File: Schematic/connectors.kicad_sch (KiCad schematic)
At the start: 36 parts, among them J10 PIN2216, J11 PIN2216, J12 PIN2216, J2 PIN2216, J3 PIN2216, J4 PIN2216, J5 PIN2216, J6 PIN2216, J7 PIN2216, J8 PIN2216, J9 PIN2216, U14 HDGC1002WR-S-4P, U15 HDGC1002WR-S-4P, U16 HDGC1002WR-S-4P, U17 HDGC1002WR-S-4P, U18 HDGC1002WR-S-4P, U19 HDGC1002WR-S-4P, U20 HDGC1002WR-S-4P, U21 HDGC1002WR-S-8P, U22 HDGC1002WR-S-8P, U23 HDGC1002WR-S-6P, U24 HDGC1002WR-S-6P

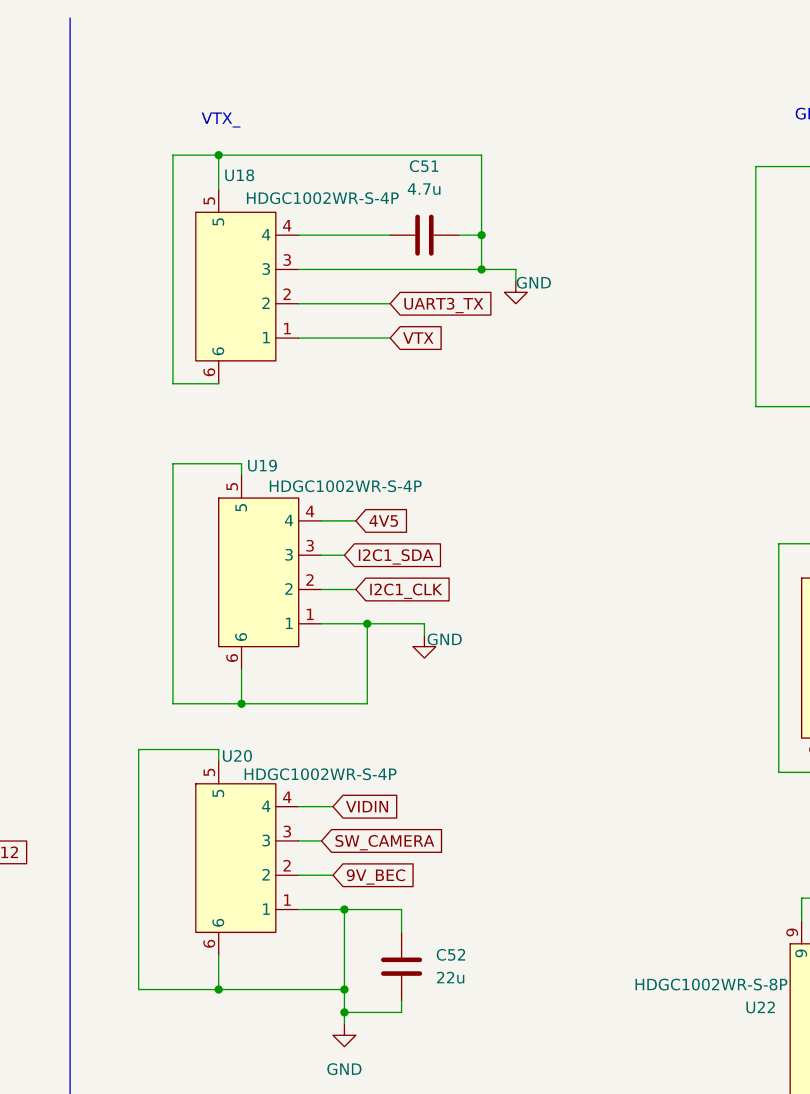
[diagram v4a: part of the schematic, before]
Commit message: Refactor schematic files and update component placements
- Adjusted component positions in osd.kicad_sch for better layout.
- Added new junctions and wires in rf_rx.kicad_sch to improve connectivity.
- Introduced additional junctions and wires in sensors.kicad_sch for enhanced signal routing.
- Removed outdated backup file fch7-2025-11-18_191836.zip and added new backup fch7-2025-11-27_202230.zip.
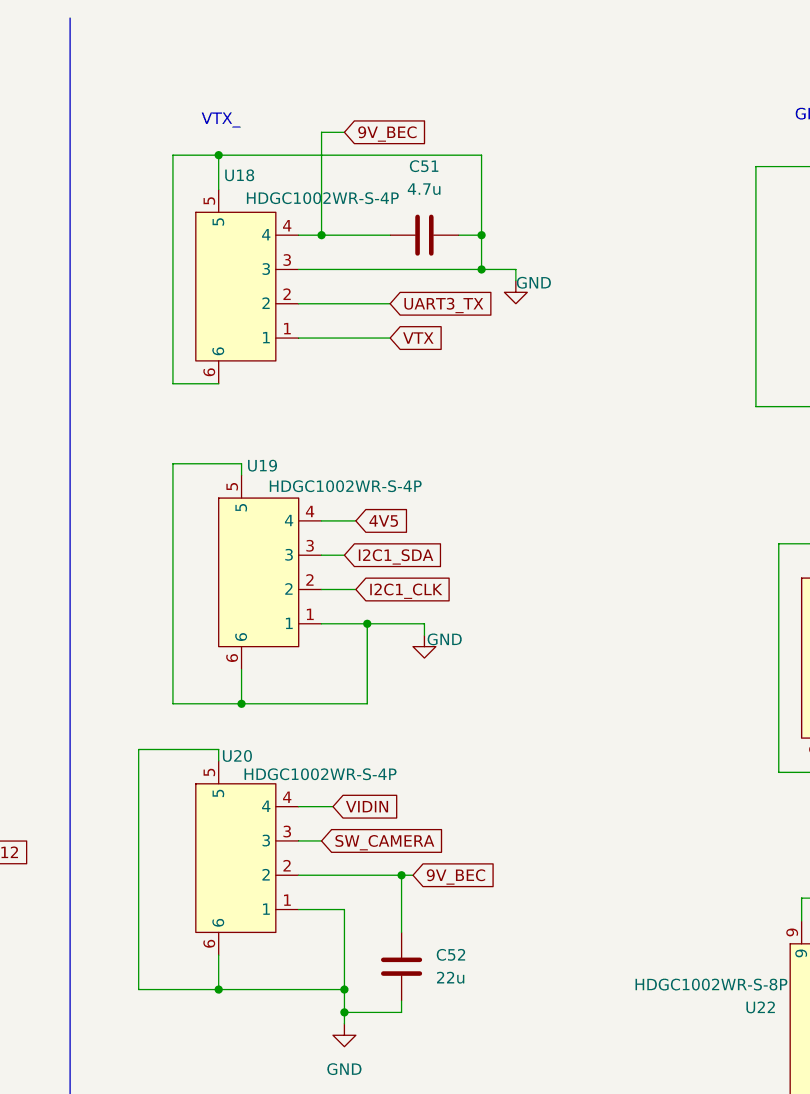
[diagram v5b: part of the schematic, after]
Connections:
- net 9V_BEC: now also C51.1, C52.2, U18.4
- net GND: no longer C52.2
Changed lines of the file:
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@@
-	)
-	(junction
-		(at 147.32 111.76)
-		(diameter 0)
-		(color 0 0 0 0)
 	)
 	(junction
@@
 	)
 	(junction
+		(at 144.78 36.83)
+		(diameter 0)
+		(color 0 0 0 0)
+	)
+	(junction
+		(at 153.67 107.95)
+		(diameter 0)
+		(color 0 0 0 0)
+	)
+	(junction
 		(at 31.75 87.63)
 		(diameter 0)
@@
 	(wire
 		(pts
-			(xy 153.67 111.76) (xy 153.67 114.3)
+			(xy 153.67 107.95) (xy 153.67 114.3)
 		)
 		(stroke
@@
 	(wire
 		(pts
+			(xy 144.78 36.83) (xy 152.4 36.83)
+		)
+		(stroke
+			(width 0)
+			(type default)
+		)
+	)
+	(wire
+		(pts
 			(xy 207.01 121.92) (xy 208.28 121.92)
 		)
@@
 	(wire
 		(pts
+			(xy 147.32 25.4) (xy 144.78 25.4)
+		)
+		(stroke
+			(width 0)
+			(type default)
+		)
+	)
+	(wire
+		(pts
 			(xy 210.82 90.17) (xy 212.09 90.17)
 		)
@@
 	(wire
 		(pts
-			(xy 142.24 107.95) (xy 146.05 107.95)
+			(xy 142.24 107.95) (xy 153.67 107.95)
 		)
 		(stroke
@@
 	(wire
 		(pts
+			(xy 144.78 25.4) (xy 144.78 36.83)
+		)
+		(stroke
+			(width 0)
+			(type default)
+		)
+	)
+	(wire
+		(pts
 			(xy 31.75 119.38) (xy 44.45 119.38)
 		)
@@
 	(wire
 		(pts
+			(xy 153.67 107.95) (xy 154.94 107.95)
+		)
+		(stroke
+			(width 0)
+			(type default)
+		)
+	)
+	(wire
+		(pts
 			(xy 153.67 143.51) (xy 153.67 146.05)
 		)
@@
 	(wire
 		(pts
-			(xy 142.24 36.83) (xy 152.4 36.83)
+			(xy 142.24 36.83) (xy 144.78 36.83)
 		)
 		(stroke
@@
 	(wire
 		(pts
-			(xy 147.32 111.76) (xy 153.67 111.76)
-		)
-		(stroke
-			(width 0)
-			(type default)
-		)
-	)
-	(wire
-		(pts
 			(xy 222.25 87.63) (xy 222.25 96.52)
 		)
@@
 		)
 	)
+	(global_label "9V_BEC"
+		(shape input)
+		(at 147.32 25.4 0)
+		(fields_autoplaced yes)
+		(effects
+			(font
+				(size 1.27 1.27)
+			)
+			(justify left)
+		)
+		(property "Intersheetrefs" "${INTERSHEET_REFS}"
+			(at 157.2599 25.4 0)
+			(effects
+				(font
+					(size 1.27 1.27)
+				)
+				(justify left)
+				(hide yes)
+			)
+		)
+	)
 	(global_label "SWD_SWCLK"
 		(shape input)
@@
 	(global_label "9V_BEC"
 		(shape input)
-		(at 146.05 107.95 0)
-		(fields_autoplaced yes)
-		(effects
-			(font
-				(size 1.27 1.27)
-			)
-			(justify left)
-		)
-		(property "Intersheetrefs" "${INTERSHEET_REFS}"
-			(at 155.9899 107.95 0)
-			(effects
-				(font
+		(at 154.94 107.95 0)
+		(fields_autoplaced yes)
+		(effects
+			(font
+				(size 1.27 1.27)
+			)
+			(justify left)
+		)
+		(property "Intersheetrefs" "${INTERSHEET_REFS}"
+			(at 164.8799 107.95 0)
+			(effects
+				(font

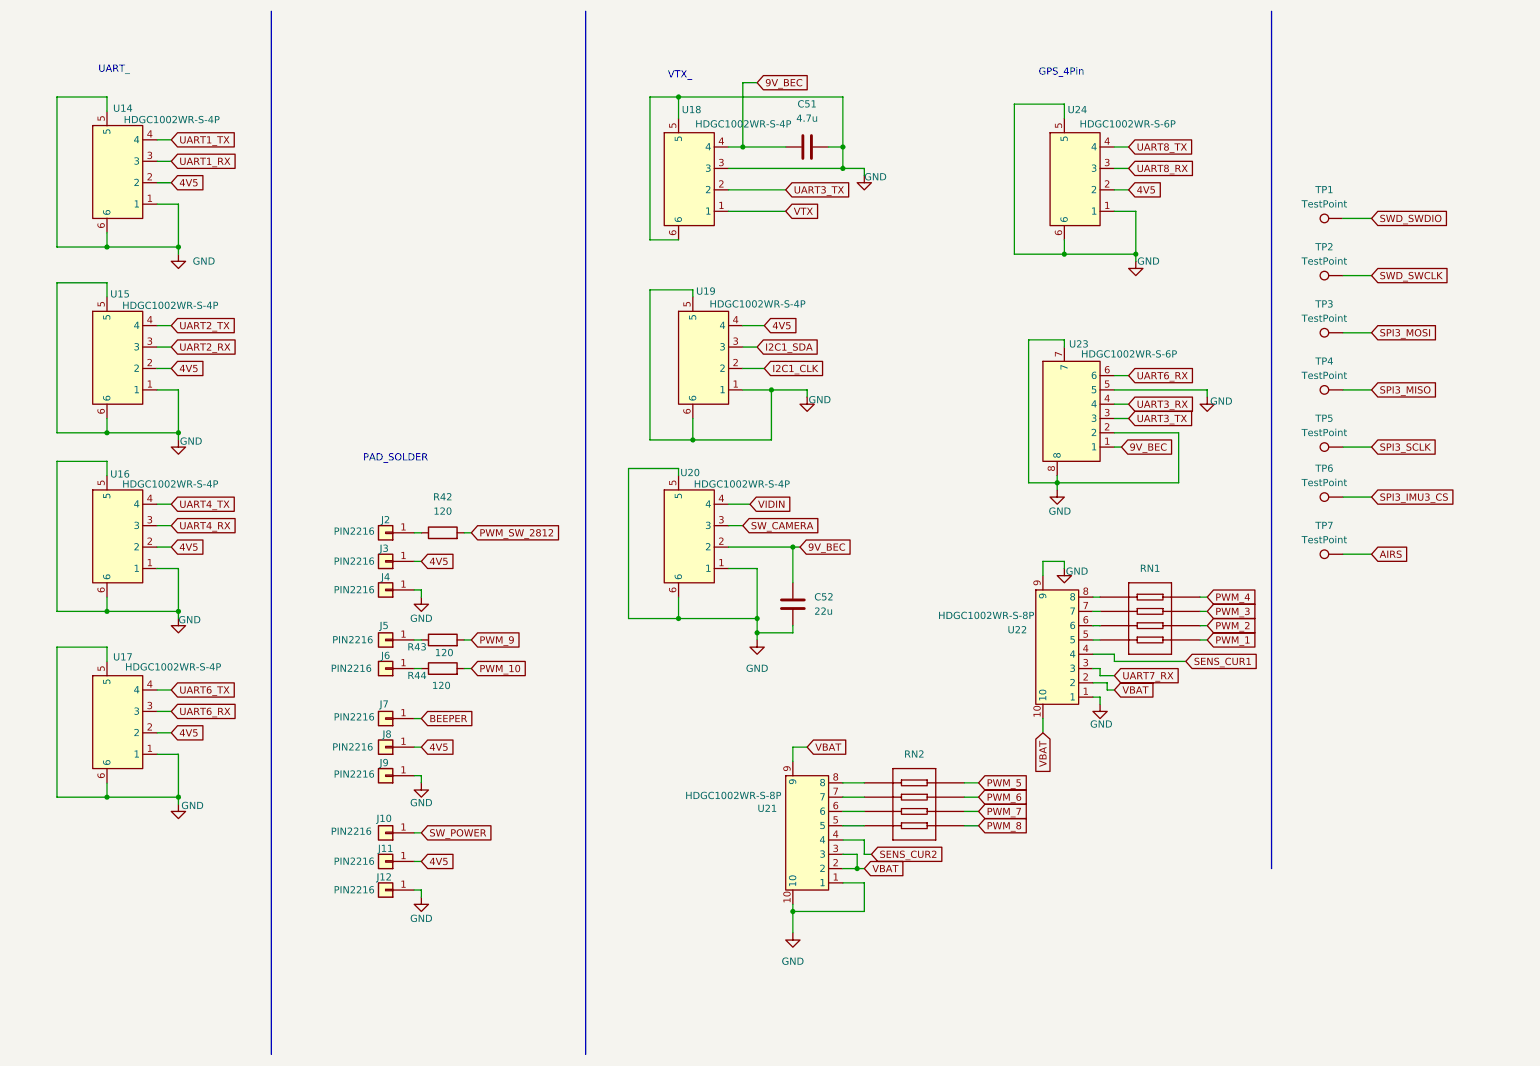
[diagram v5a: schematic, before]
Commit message: Removed useless analog OSD and VTX conneections to support only digital DJI
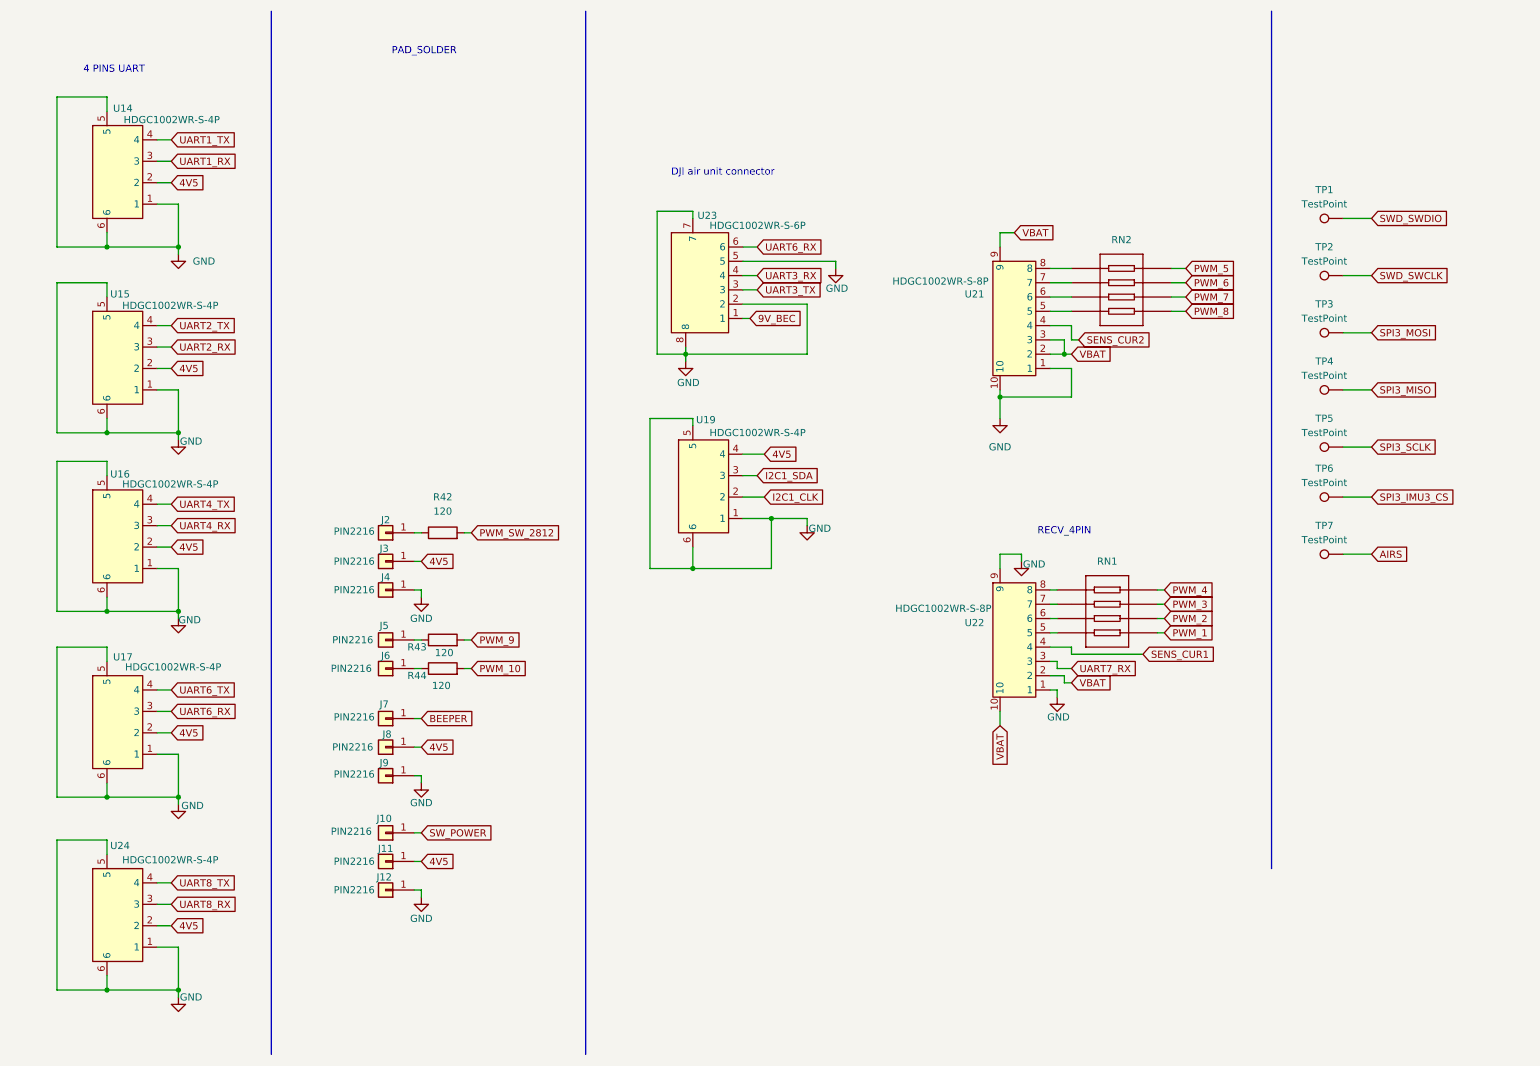
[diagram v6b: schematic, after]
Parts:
- removed C51: 4.7u, Capacitor_SMD:C_0603_1608Metric, symbol Device:C
- removed C52: 22u, Capacitor_SMD:C_0805_2012Metric, symbol Device:C
- removed U18, U20: HDGC1002WR-S-4P, fch7_fp:SM03B-SRSS-TB(LF)(SN), symbol fclib:HDGC1002WR-S-4P
- U24: value HDGC1002WR-S-6P -> HDGC1002WR-S-4P; footprint fch7_fp:CONN-SMD_HDGC1002WR-S-6P -> fch7_fp:SM03B-SRSS-TB(LF)(SN)
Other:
- note added: "4 PINS UART"
- note added: "DJI air unit connector"
- note added: "RECV_4PIN"
- note removed: "GPS_4Pin"
- note removed: "UART_"
- note removed: "VTX_"
- moved on the sheet: RN1, RN2, U19, U21, U22, U23, U24

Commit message: refactor : improve readability and portability of the project
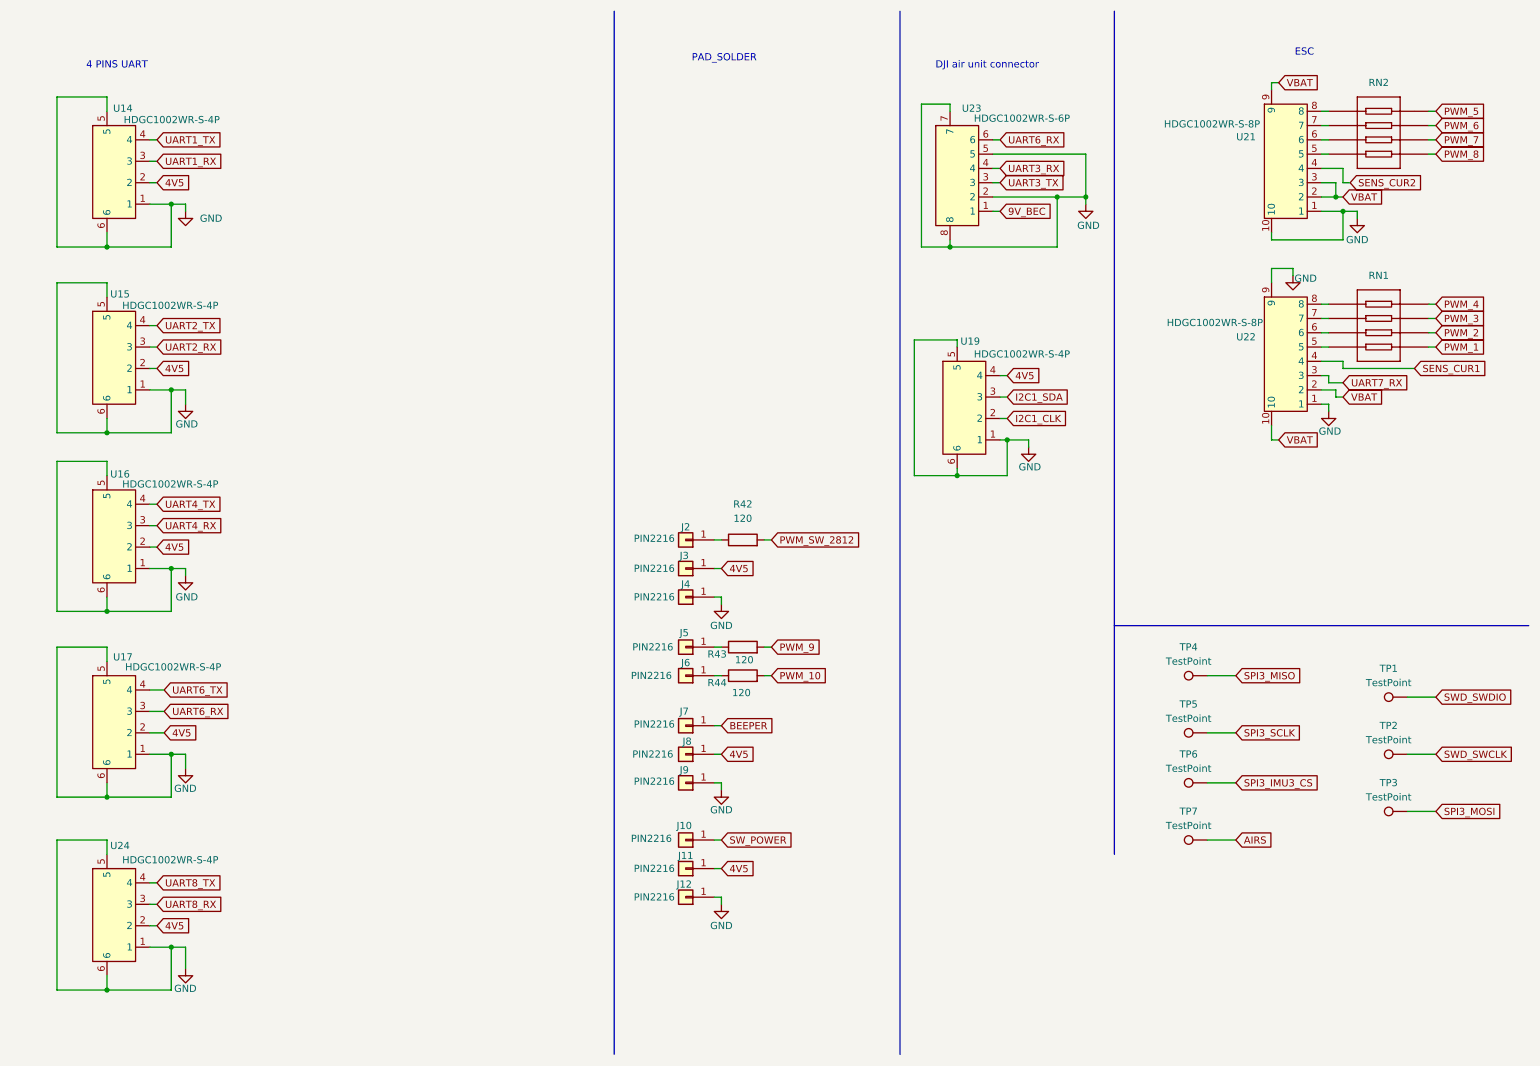
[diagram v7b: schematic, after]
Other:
- note added: "ESC"
- note removed: "RECV_4PIN"
- moved on the sheet: J10, J11, J12, J2, J3, J4, J5, J6, J7, J8, J9, R42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

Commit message: zdd :minor improvements
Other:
- note added: "Debugging"
- note added: "Vérifier l'ordre des pins pour le connecteur ESC"
- moved on the sheet: RN1, RN2, TP1, TP2, TP3, TP4, TP5, TP6, TP7, U21, U22
